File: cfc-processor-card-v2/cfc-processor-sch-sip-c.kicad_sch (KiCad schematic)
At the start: 49 parts, among them J5 DM3BT-DSF-PEJS, U11 TCAN330, U12 SFEM016GB1EA1TO-I-GE-121-STD, U7 OSD3358-1G-ISM

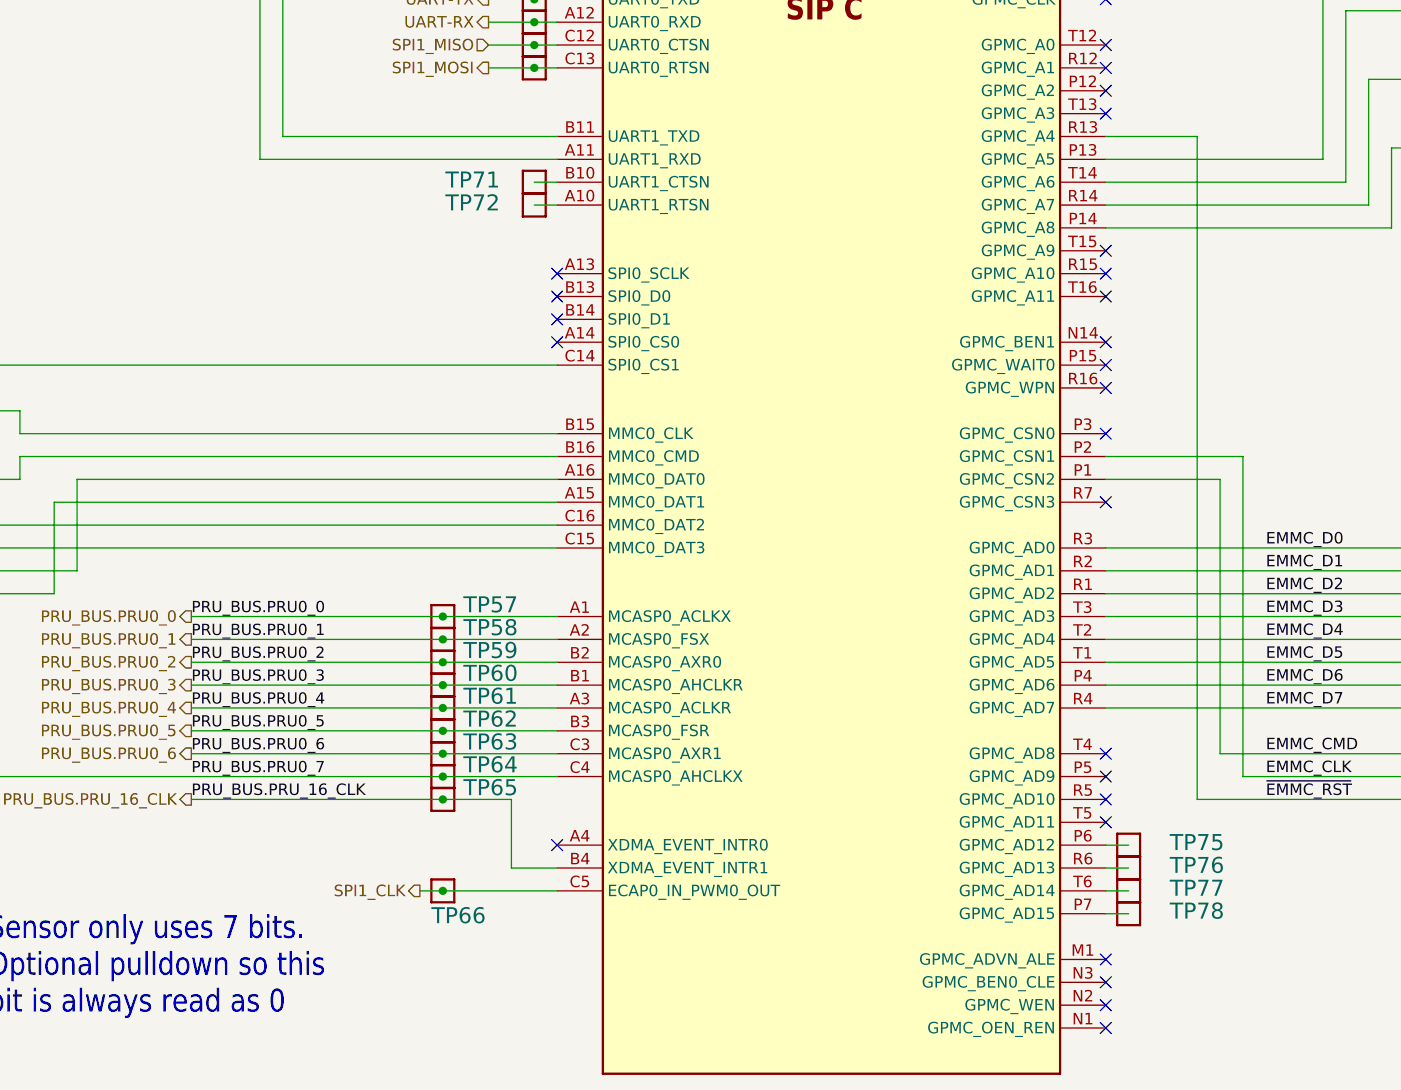
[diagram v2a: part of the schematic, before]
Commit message: Update
Added pull down resistors and removed therm + and sensor enable and added i2c support for cfc sensor card.
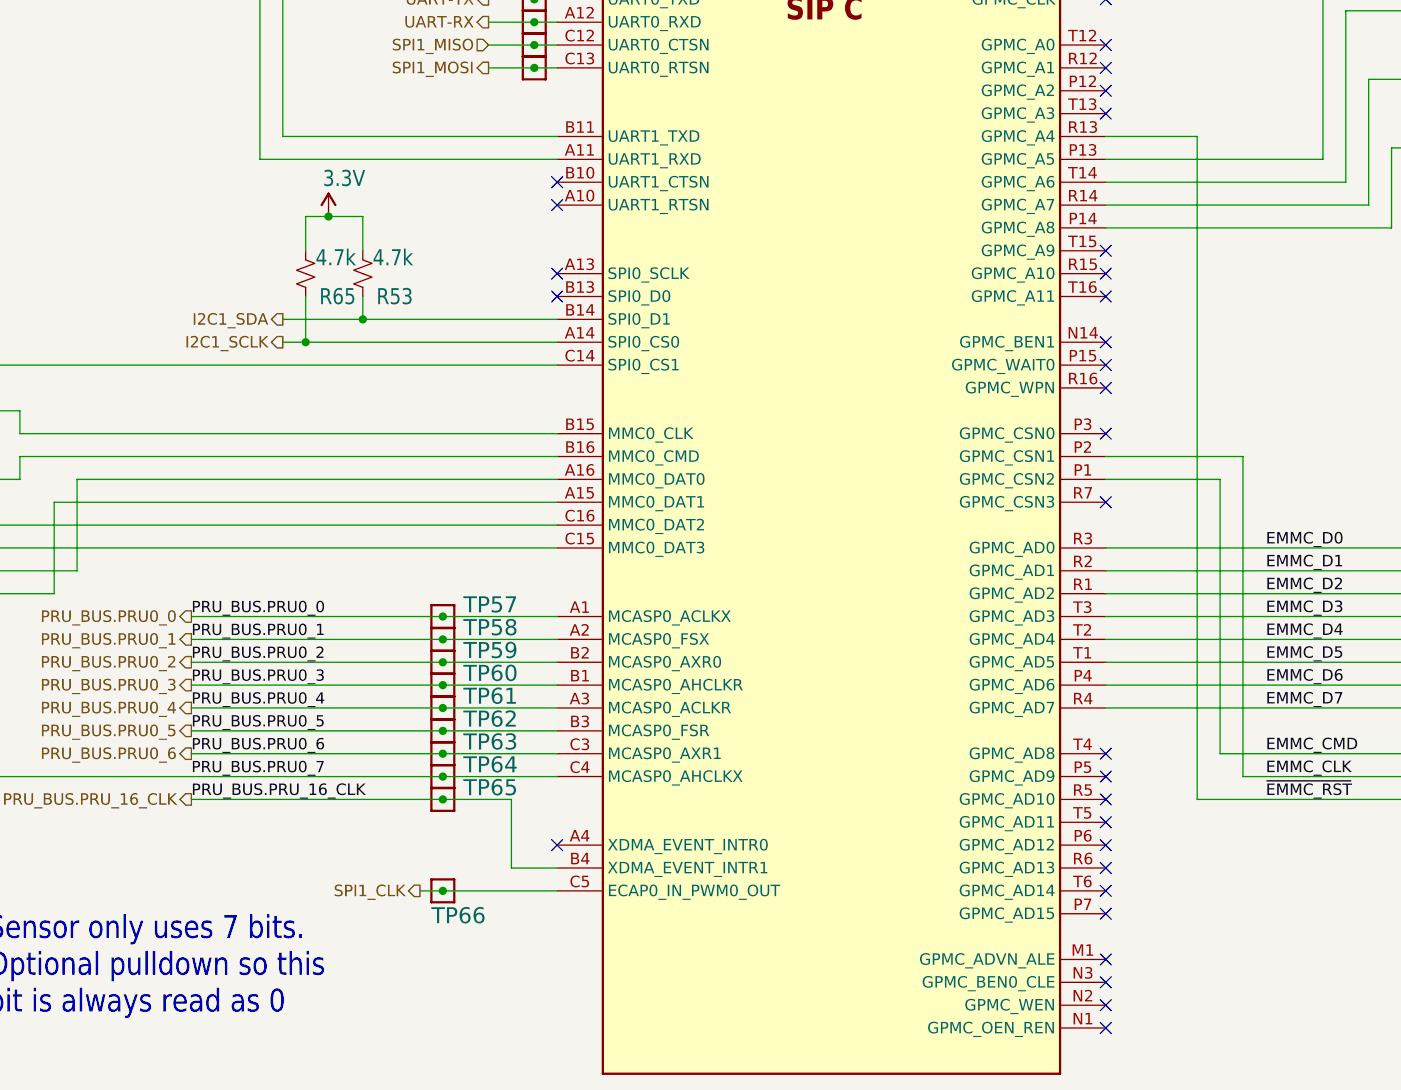
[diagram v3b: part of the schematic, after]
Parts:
- removed TP71, TP72, TP75, TP76, TP77, TP78: TEST-POINT3X4, oresat-misc:TestPoint_Pad_D1.0mm, symbol Oresat Misc:Test-Point-1mm-round
- added R53, R65: 4.7k, oresat-passives:0603-C-NOSILK, symbol Device:R_Small_US
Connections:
- net 3.3V: now also R53.2, R65.2
- net I2C1_SCLK: now reaches U7.A14 (SPI0_CS0)
- net I2C1_SCLK: now also R65.1
- net I2C1_SDA: now reaches U7.B14 (SPI0_D1)
- net I2C1_SDA: now also R53.1
- no-connect marks 32 -> 36

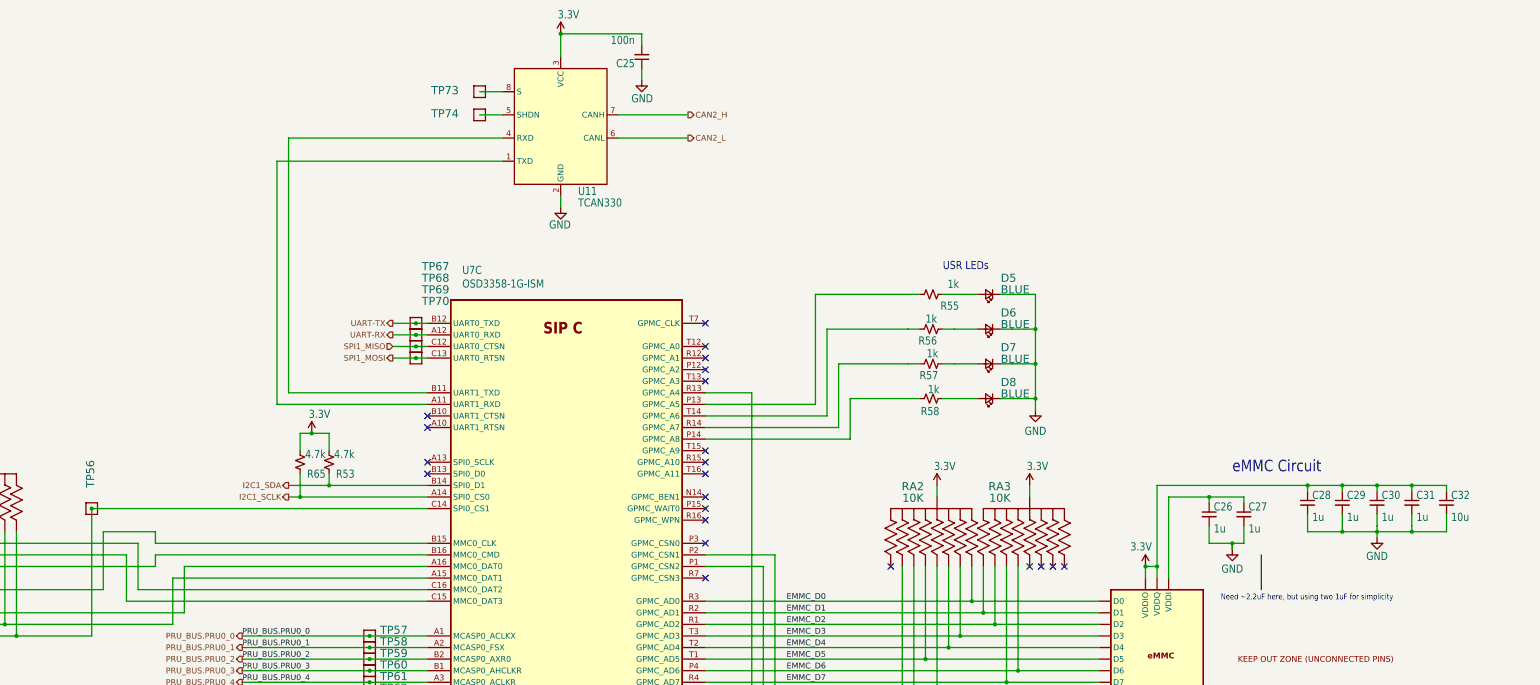
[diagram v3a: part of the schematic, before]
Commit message: Update
Fixed a couple of library issues on testpoints and other misc components. Added Pull up resistors to 8 channel i2c ic
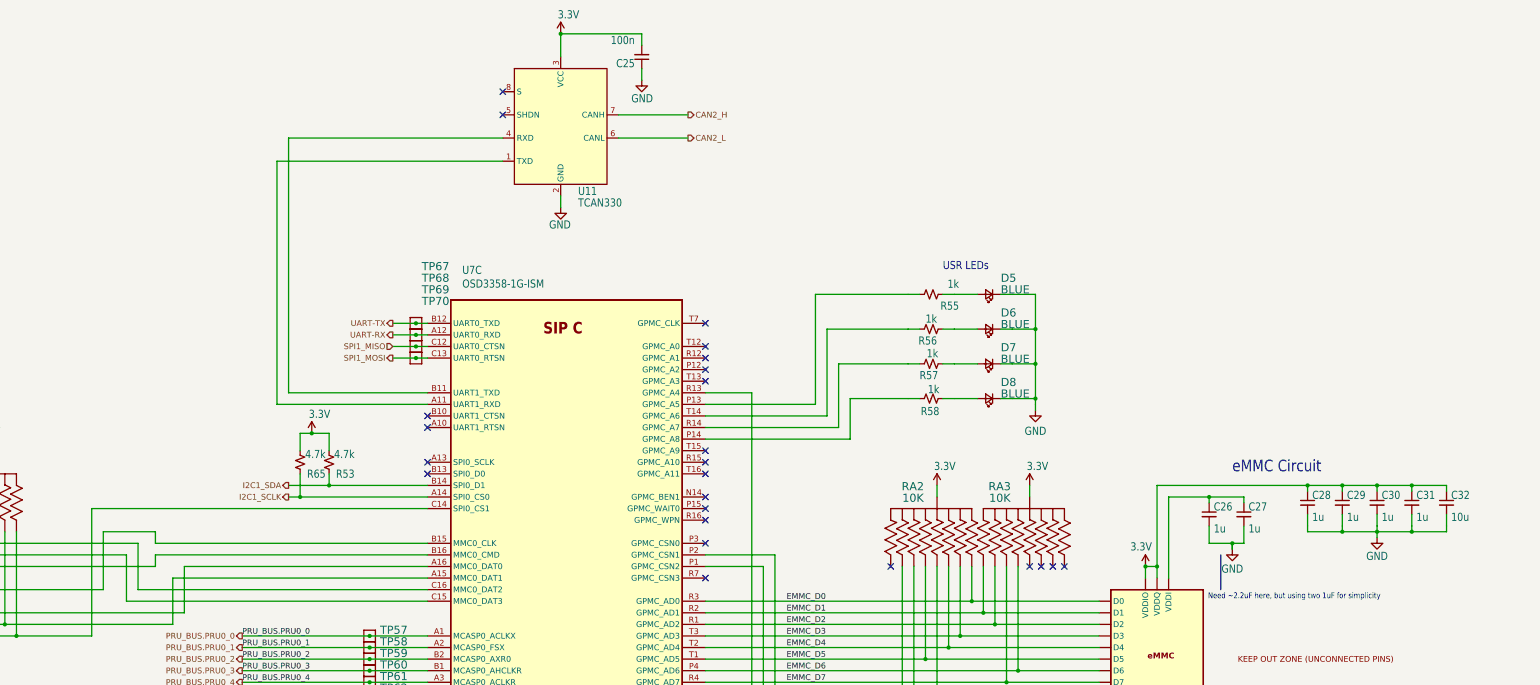
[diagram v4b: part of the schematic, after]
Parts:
- removed TP56, TP73, TP74: TEST-POINT3X4, oresat-misc:TestPoint_Pad_D1.0mm, symbol Oresat Misc:Test-Point-1mm-round
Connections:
- no-connect marks 36 -> 38

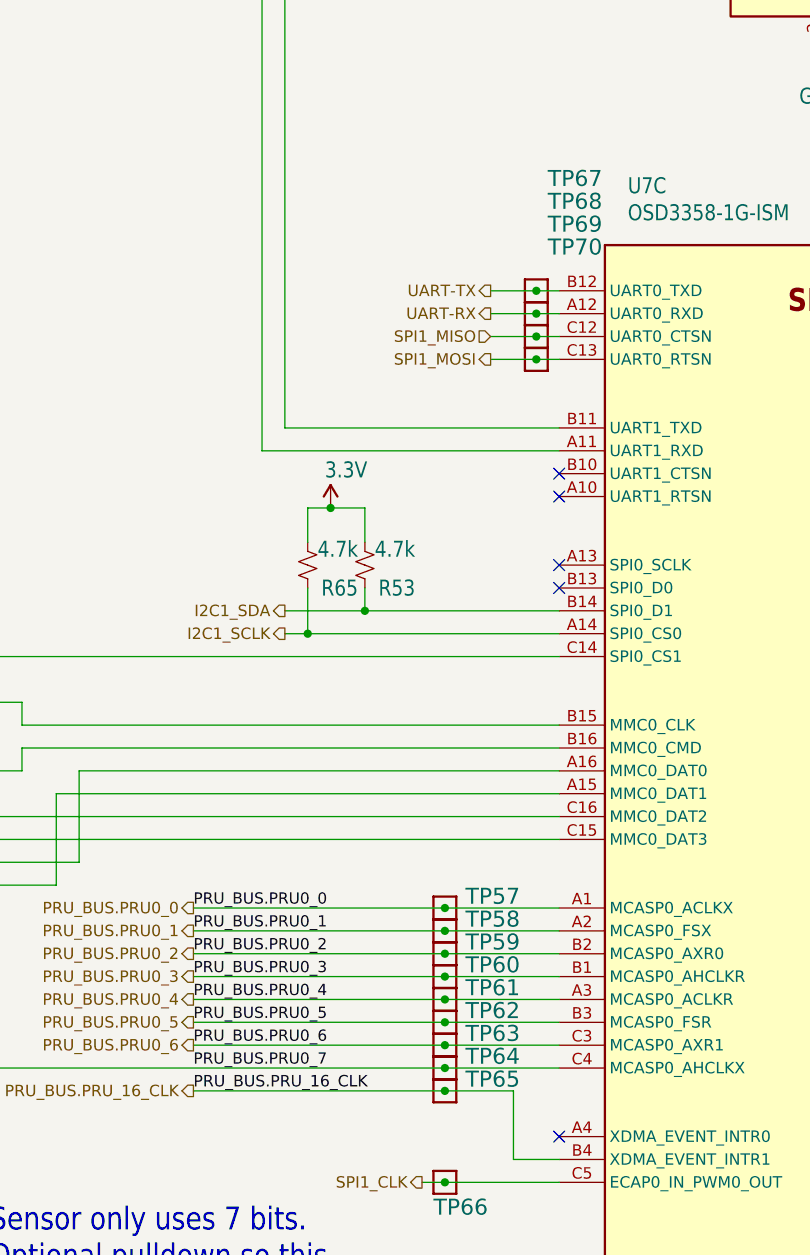
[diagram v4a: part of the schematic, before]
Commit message: update
Changed a couple of test points on OPD to through hole test points. Added tables to DRV8212 on sensor schematic+ other visual improvements to processor schematic.
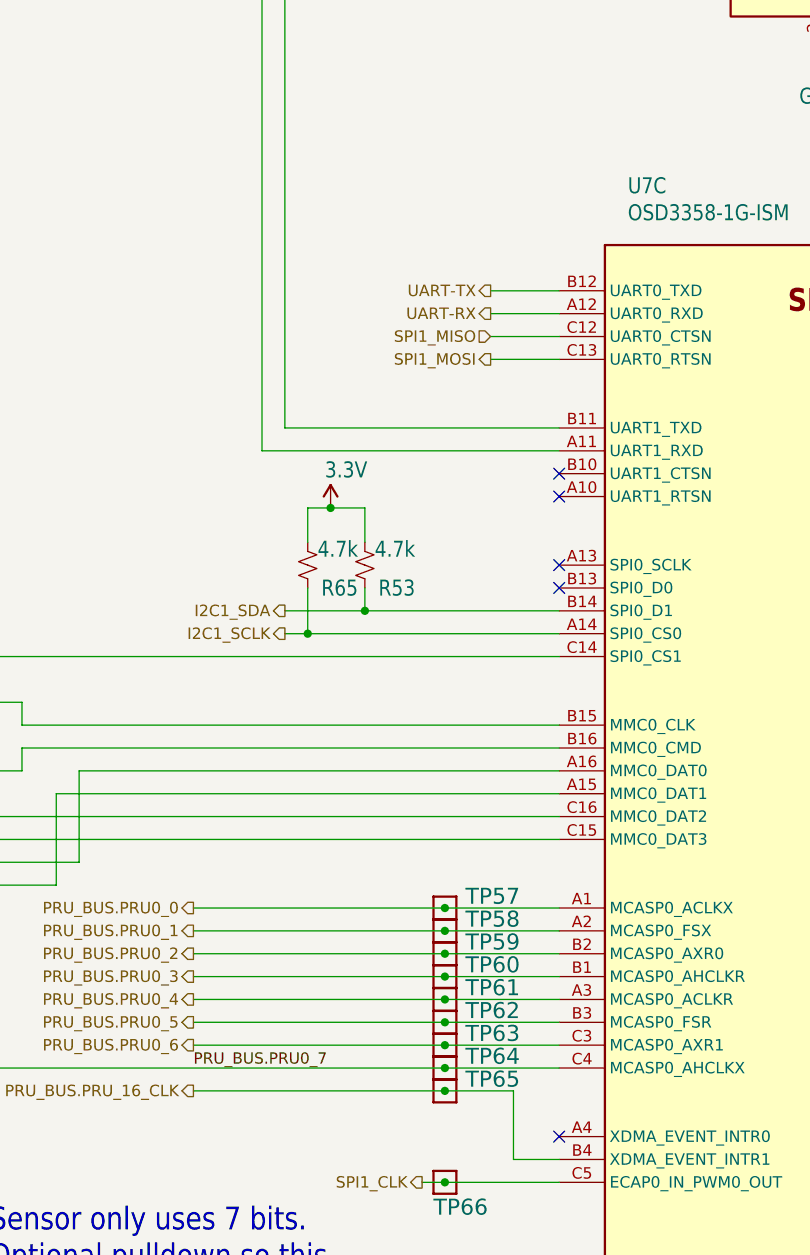
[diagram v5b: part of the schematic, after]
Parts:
- removed TP67, TP68, TP69, TP70: TEST-POINT, cfc-card:2MM-TEST-POINT, symbol cfc-card-eagle-import:TEST-POINT
